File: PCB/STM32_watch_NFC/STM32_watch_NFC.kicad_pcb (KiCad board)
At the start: 2 copper layers, 40 x 40 mm, 68 parts, among them J1 Conn_01x06_Socket, J2 USB_C_Receptacle_PowerOnly_6P, Q1 2N7000, SW1 SW_DPST_x2, SW2 SW_DPST_x2, SW3 SW_DPST_x2, U1 STM32L031G6Ux, U2 MIC5365-3.3YC5, U3 ST25R3916-AQWT, U4 MT3608

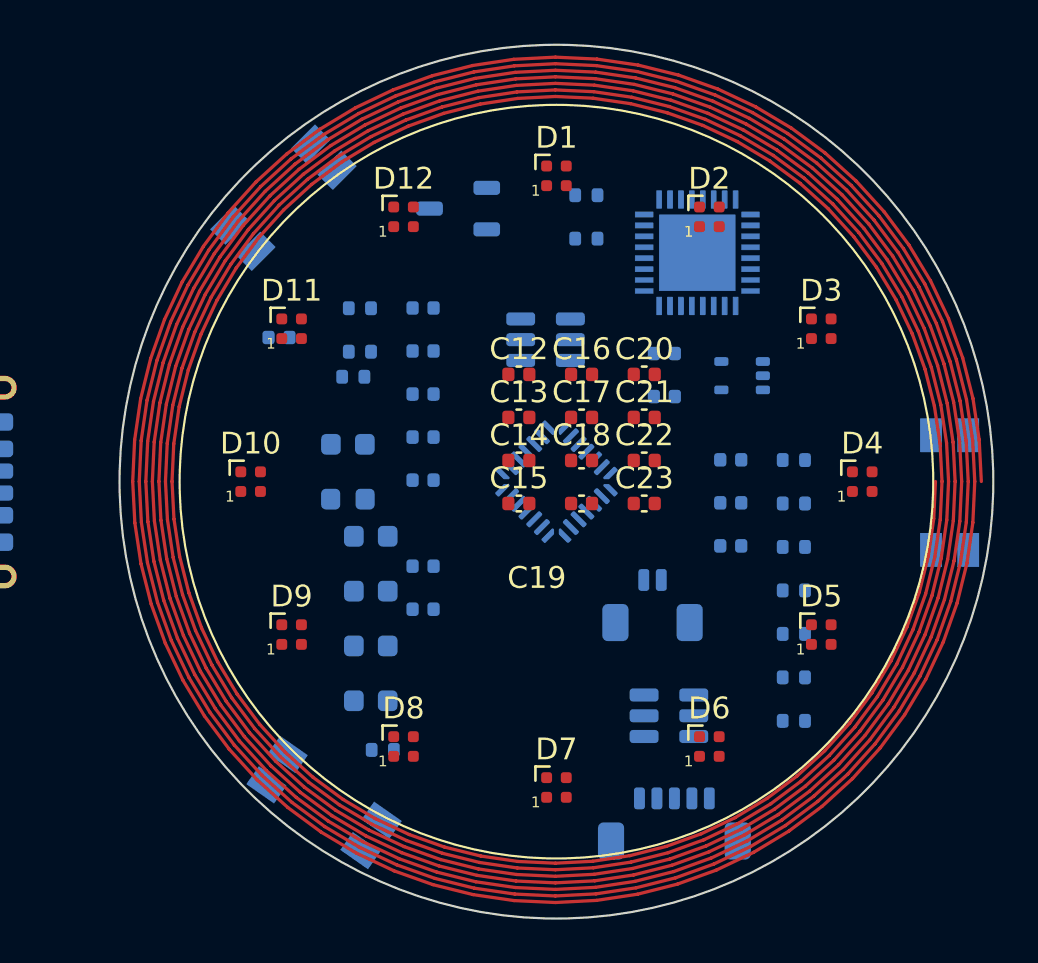
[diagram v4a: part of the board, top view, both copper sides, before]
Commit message: NFC antenna - Kicad
I hope that antenna will work - I used TI coil designer, st25r - antenna tunning program and lots of datasheets/aplication notes
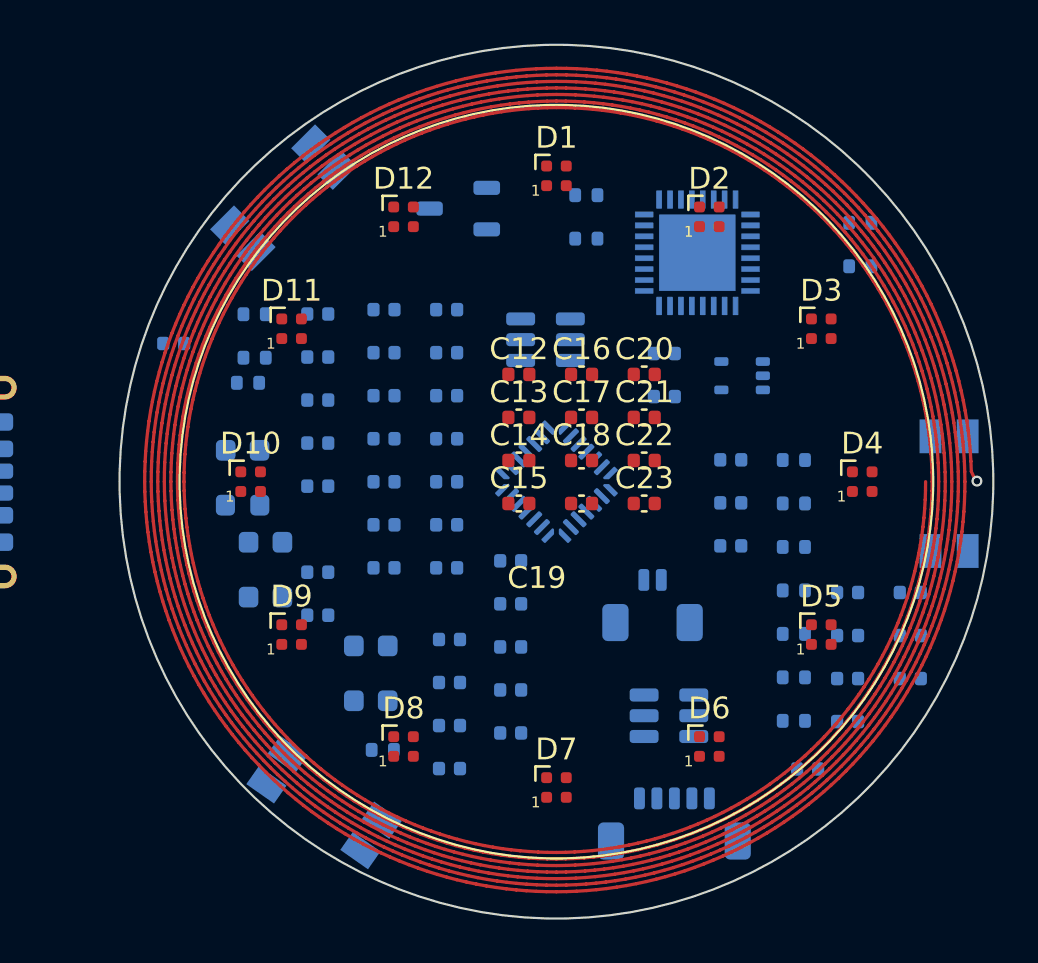
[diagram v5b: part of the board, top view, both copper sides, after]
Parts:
- added C31: 100n, Capacitor_SMD:C_0402_1005Metric, B.Cu at (143.5, 97.1)
- added C32: 22n, Capacitor_SMD:C_0402_1005Metric, B.Cu at (143.5, 99.1)
- added C33: 2.2uF, Capacitor_SMD:C_0402_1005Metric, B.Cu at (143.5, 101.1)
- added C34: 22n, Capacitor_SMD:C_0402_1005Metric, B.Cu at (143.5, 103.0)
- added C35: 2.2uF, Capacitor_SMD:C_0402_1005Metric, B.Cu at (143.5, 105.0)
- added C36: 22n, Capacitor_SMD:C_0402_1005Metric, B.Cu at (143.5, 107.0)
- added C37: 2.2uF, Capacitor_SMD:C_0402_1005Metric, B.Cu at (143.5, 108.9)
- added C38: 22n, Capacitor_SMD:C_0402_1005Metric, B.Cu at (140.6, 97.1)
- added C39: 2.2uF, Capacitor_SMD:C_0402_1005Metric, B.Cu at (140.6, 99.1)
- added C40: 22n, Capacitor_SMD:C_0402_1005Metric, B.Cu at (140.6, 101.1)
- added C41: 2.2uF, Capacitor_SMD:C_0402_1005Metric, B.Cu at (140.6, 103.0)
- added C42: 22n, Capacitor_SMD:C_0402_1005Metric, B.Cu at (140.6, 105.0)
- added C43: 2.2uF, Capacitor_SMD:C_0402_1005Metric, B.Cu at (140.6, 107.0)
- added C44: 22n, Capacitor_SMD:C_0402_1005Metric, B.Cu at (140.6, 108.9)
- added C45: 2.2uF, Capacitor_SMD:C_0402_1005Metric, B.Cu at (146.4, 108.6)
- added C46: 1u, Capacitor_SMD:C_0402_1005Metric, B.Cu at (146.4, 110.6)
- added C47: 22n, Capacitor_SMD:C_0402_1005Metric, B.Cu at (146.4, 112.6)
- added C48: 15pF, Capacitor_SMD:C_0402_1005Metric, B.Cu at (146.4, 114.5)
- added C49: 15pF, Capacitor_SMD:C_0402_1005Metric, B.Cu at (146.4, 116.5)
- added C50: 15pF, Capacitor_SMD:C_0402_1005Metric, B.Cu at (143.6, 112.2)
- added C51: 15pF, Capacitor_SMD:C_0402_1005Metric, B.Cu at (143.6, 114.2)
- added C52: 220pF, Capacitor_SMD:C_0402_1005Metric, B.Cu at (143.6, 116.2)
- added C53: 220pF, Capacitor_SMD:C_0402_1005Metric, B.Cu at (143.6, 118.1)
- added C54: 220pF, Capacitor_SMD:C_0402_1005Metric, B.Cu at (164.7, 110.1)
- added C55: 220pF, Capacitor_SMD:C_0402_1005Metric, B.Cu at (164.7, 112.0)
- added C56: 10pF, Capacitor_SMD:C_0402_1005Metric, B.Cu at (164.7, 114.0)
- added C57: 220pF, Capacitor_SMD:C_0402_1005Metric, B.Cu at (160.0, 118.2)
- added C58: 15pF, Capacitor_SMD:C_0402_1005Metric, B.Cu at (161.8, 110.1)
- added C59: 15pF, Capacitor_SMD:C_0402_1005Metric, B.Cu at (161.8, 112.0)
- added C60: 10pF, Capacitor_SMD:C_0402_1005Metric, B.Cu at (161.8, 114.0)
- added C61: 220pF, Capacitor_SMD:C_0402_1005Metric, B.Cu at (161.8, 116.0)
- added R16: 10K, Resistor_SMD:R_0402_1005Metric, B.Cu at (162.4, 93.2)
- added R17: 10K, Resistor_SMD:R_0402_1005Metric, B.Cu at (162.4, 95.1)
- moved C7 4.83 mm to (131.0, 98.7)
- moved C1 4.83 mm to (137.6, 97.3)
- moved C2 4.83 mm to (137.6, 99.3)
- moved C24 4.83 mm to (135.2, 107.8)
- moved C25 4.83 mm to (135.2, 110.3)
- moved C3 4.83 mm to (137.6, 101.3)
- moved C4 4.83 mm to (134.1, 103.6)
- moved C5 4.83 mm to (137.6, 103.2)
- moved C6 4.83 mm to (137.6, 105.2)
- moved C8 4.83 mm to (137.6, 109.1)
- moved C9 4.83 mm to (137.6, 111.1)
- moved FB1 4.83 mm to (134.1, 106.1)
- moved R1 4.83 mm to (134.7, 97.3)
- moved R2 4.83 mm to (134.7, 99.3)
- moved R3 4.83 mm to (134.4, 100.5)
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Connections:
- U1 pad 10: unconnected-(U1-PA4-Pad10) -> SPI_CS_STM
- U1 pad 11: unconnected-(U1-PA5-Pad11) -> SPI_SCL_STM
- U1 pad 12: unconnected-(U1-PA6-Pad12) -> SPI_MISO_STM
- U1 pad 13: unconnected-(U1-PA7-Pad13) -> SPI_MOSI_STM
- U1 pad 9: unconnected-(U1-PA3-Pad9) -> SPI_IRQ_STM
- U3 pad 1: unconnected-(U3-VDD_IO-Pad1) -> +3.3V
- U3 pad 10: unconnected-(U3-VDD_TX-Pad10) -> +5V
- U3 pad 11: unconnected-(U3-VDD_AM-Pad11) -> Net-(U3-VDD_AM)
- U3 pad 12: Net-(U3-GND_DR-Pad12) -> GND
- U3 pad 13: unconnected-(U3-RFO1-Pad13) -> Net-(U3-RFO1)
- U3 pad 14: unconnected-(U3-VDD_DR-Pad14) -> Net-(U3-VDD_DR)
- U3 pad 15: unconnected-(U3-RFO2-Pad15) -> Net-(U3-RFO2)
- U3 pad 16: Net-(U3-GND_DR-Pad12) -> GND
- U3 pad 20: unconnected-(U3-I2C_EN-Pad20) -> GND
- U3 pad 21: unconnected-(U3-VSS-Pad21) -> GND
- U3 pad 22: unconnected-(U3-RFI1-Pad22) -> Net-(U3-RFI1)
- U3 pad 23: unconnected-(U3-RFI2-Pad23) -> Net-(U3-RFI2)
- U3 pad 24: unconnected-(U3-AGDC-Pad24) -> Net-(U3-AGDC)
- U3 pad 26: unconnected-(U3-GND_A-Pad26) -> GND
- U3 pad 27: unconnected-(U3-IRQ-Pad27) -> SPI_IRQ_STM
- U3 pad 29: unconnected-(U3-~{BSS}-Pad29) -> SPI_CS_STM
- U3 pad 3: unconnected-(U3-VDD_D-Pad3) -> Net-(U3-VDD_D)
- U3 pad 30: unconnected-(U3-SCLK/SCL-Pad30) -> SPI_SCL_STM
- U3 pad 31: unconnected-(U3-MOSI-Pad31) -> SPI_MOSI_STM
- U3 pad 32: unconnected-(U3-MISO/SDA-Pad32) -> SPI_MISO_STM
- U3 pad 33: unconnected-(U3-EXP-Pad33) -> GND
- U3 pad 4: unconnected-(U3-XTO-Pad4) -> Net-(U3-XTO)
- U3 pad 5: unconnected-(U3-XTI-Pad5) -> Net-(U3-XTI)
- U3 pad 6: unconnected-(U3-GND_D-Pad6) -> GND
- U3 pad 7: unconnected-(U3-VDD_A-Pad7) -> Net-(U3-VDD_A)
- U3 pad 8: unconnected-(U3-VDD-Pad8) -> +5V
- U3 pad 9: unconnected-(U3-VDD_RF-Pad9) -> Net-(U3-VDD_DR)
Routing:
- net unconnected-(U4-NC-Pad6): track 811.2 -> 789.5 mm
- net /NFC_RFID/A1: vias 0 -> 1

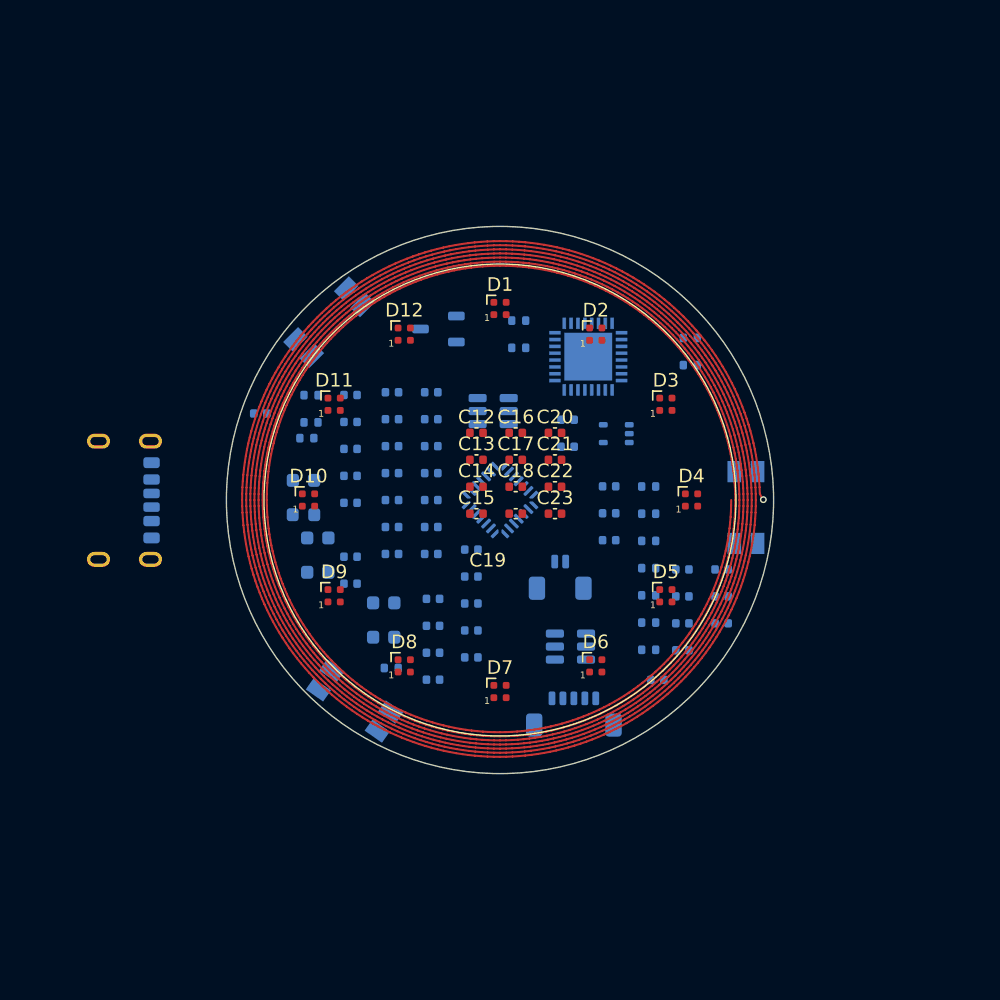
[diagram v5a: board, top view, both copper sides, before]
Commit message: Kicad - LCSC, footprints
I managed to add all (I hope so :) ) LCSC values - which component will be used. With that I could determine all footprints
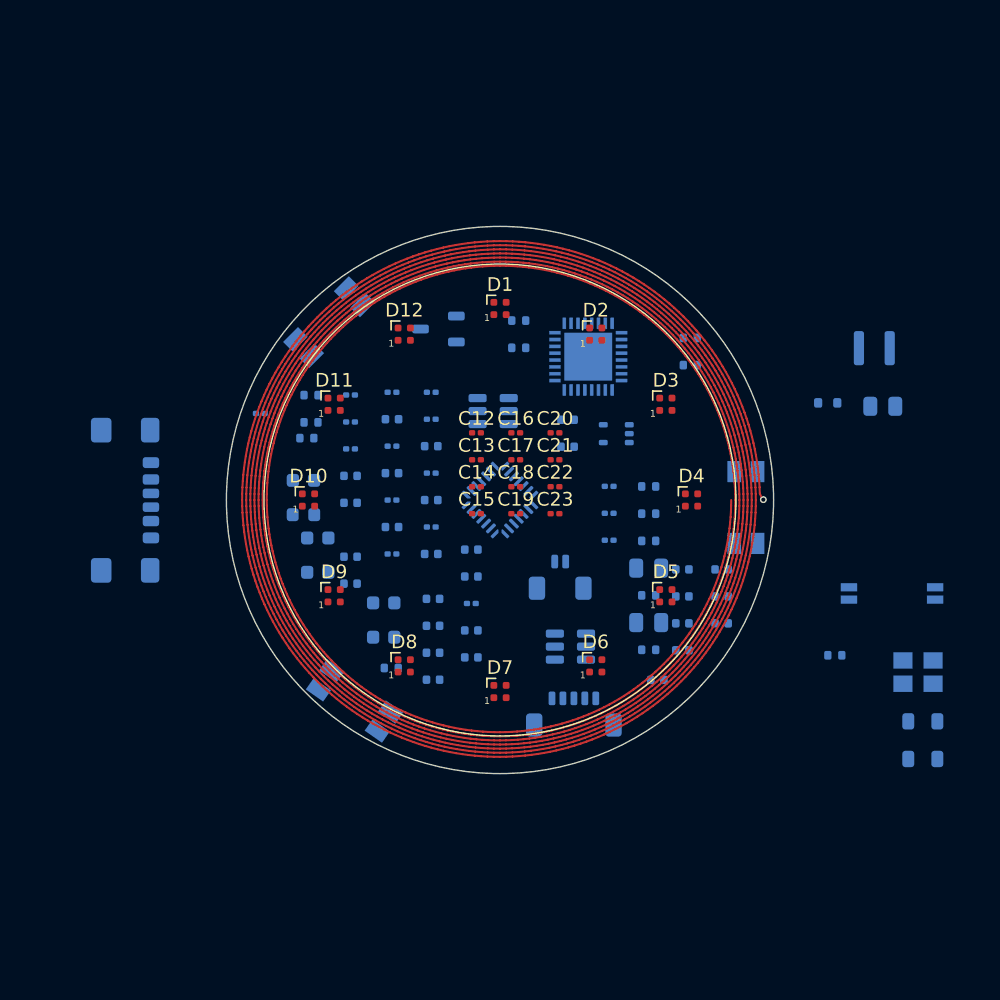
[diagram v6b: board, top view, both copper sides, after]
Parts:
- added D13: D_Schottky, Diode_SMD:D_SOD-523, B.Cu at (172.5, 97.9)
- added L1: 22uH, Components:SLW3015, B.Cu at (175.9, 93.9)
- added L2: 270nH 500mOhm, Inductor_SMD:L_0805_2012Metric, B.Cu at (179.4, 121.2)
- added L3: 270nH 500mOhm, Inductor_SMD:L_0805_2012Metric, B.Cu at (179.4, 123.9)
- added R8: 16.5K, Resistor_SMD:R_0805_2012Metric, B.Cu at (176.5, 98.2)
- added R9: 2.2K, Resistor_SMD:R_0402_1005Metric, B.Cu at (173.0, 116.3)
- added Y1: 27.12Mhz, Crystal:Crystal_SMD_3225-4Pin_3.2x2.5mm, B.Cu at (179.1, 117.6)
- added Y2: 32.768kHz, Crystal:Crystal_SMD_SeikoEpson_MC146-4Pin_6.7x1.5mm, B.Cu at (177.2, 111.8)
- C1, C12, C13, C14, C15, C16, C17, C18, C19, C2, C20, C21, C22, C23, C28, C29, C3, C30, C31, C32, C34, C36, C38, C40, C42, C44, C47, C7: footprint Capacitor_SMD:C_0402_1005Metric -> Capacitor_SMD:C_0201_0603Metric
- C26, C27: value 22u -> 10u
- J2: footprint Connector_USB:USB_C_Receptacle_GCT_USB4125-xx-x-0190_6P_TopMnt_Horizontal -> Connector_USB:USB_C_Receptacle_GCT_USB4135-GF-A_6P_TopMnt_Horizontal
- R11, R15, R6: value 500 -> 510
- R12, R14: footprint Resistor_SMD:R_0402_1005Metric -> Resistor_SMD:R_0805_2012Metric

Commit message: Kicad - layout
I placed all components in logical way. It is NOT routed.
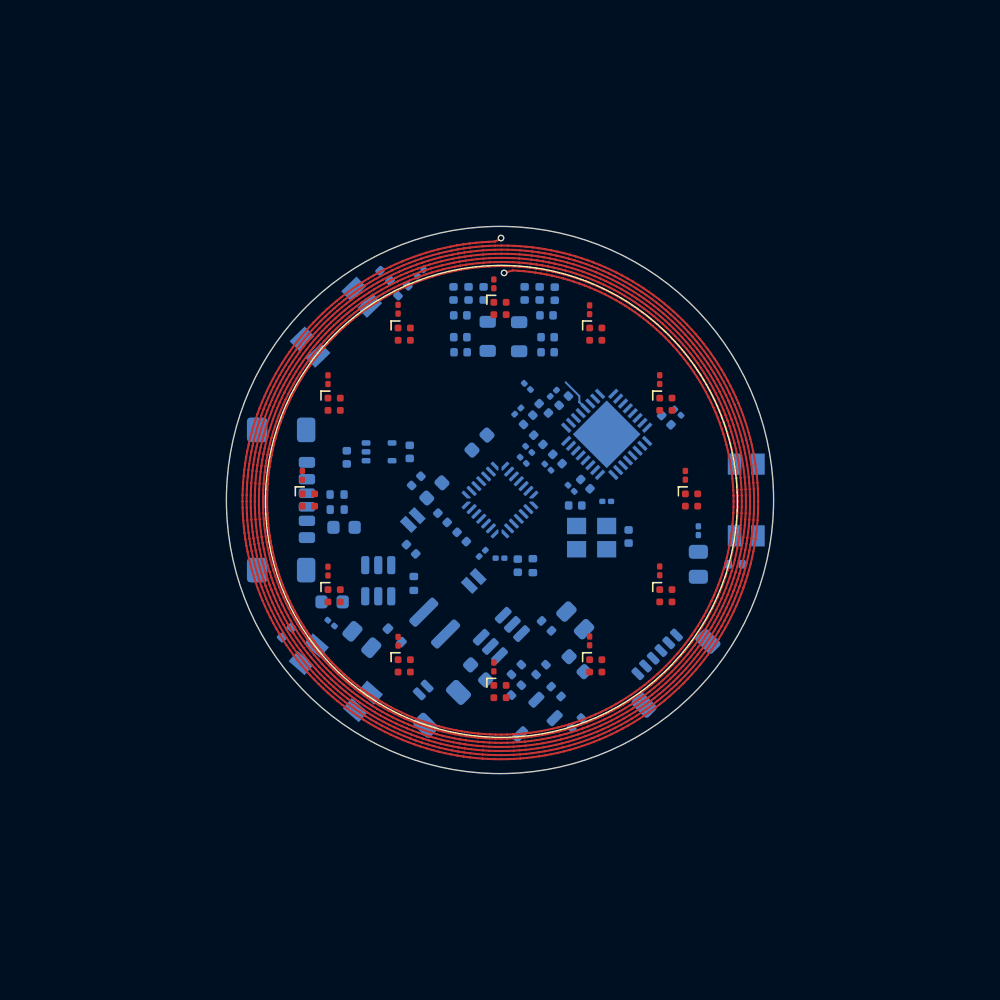
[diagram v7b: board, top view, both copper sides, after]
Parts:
- removed C32: 22n, Capacitor_SMD:C_0201_0603Metric
- removed C33: 2.2uF, Capacitor_SMD:C_0402_1005Metric
- C3: footprint Capacitor_SMD:C_0201_0603Metric -> Capacitor_SMD:C_0402_1005Metric
- J1: footprint Connector_JST:JST_SUR_SM05B-SURS-TF_1x05-1MP_P0.80mm_Horizontal -> Connector_JST:JST_SUR_SM06B-SURS-TF_1x06-1MP_P0.80mm_Horizontal
- moved L3 44.3 mm to (147.6, 93.0), turned to -90 degrees
- moved L2 40.8 mm to (149.9, 93.1), turned to 90 degrees
- moved L1 37.9 mm to (143.7, 114.0), turned to -45 degrees
- moved D13 35.9 mm to (140.8, 114.9), turned to -45 degrees
- moved SW2 33.2 mm to (166.5, 105.0), turned to 90 degrees
- moved Y2 33.0 mm to (144.4, 108.7), turned to 135 degrees
- moved SW1 32.5 mm to (136.5, 118.0), turned to -41 degrees
- moved C56 30.4 mm to (146.2, 89.9), turned to 90 degrees
- moved C57 30.3 mm to (145.6, 91.5), turned to 0 degrees
- moved Q1 29.5 mm to (150.9, 121.2), turned to -135 degrees
- moved R2 29.3 mm to (154.1, 121.3), turned to -135 degrees
- moved R1 28.1 mm to (152.6, 119.0), turned to 135 degrees
- moved SW3 27.7 mm to (136.5, 92.0), turned to -136 degrees
- moved R8 27.4 mm to (154.0, 113.8), turned to 135 degrees
- moved R16 27.4 mm to (149.7, 117.4), turned to 45 degrees
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- renumbered C17 to C12, C20 to C13, C21 to C14, C13 to C15, C14 to C16, C23 to C17, C22 to C18, C18 to C19, C15 to C20, C19 to C21, C12 to C22, C16 to C23
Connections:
- D12 pad 1: unconnected-(D12-DOUT-Pad1) -> Net-(D1-DIN)
- D6 pad 1: Net-(D6-DOUT) -> unconnected-(D6-DOUT-Pad1)
- D7 pad 3: Net-(D6-DOUT) -> Net-(D7-DIN)
- R6 pad 2: Net-(D1-DIN) -> Net-(D7-DIN)
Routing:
- net Net-(U3-RFO1): track 0.00 -> 2.50 mm
- net /NFC_RFID/A2: vias 0 -> 1
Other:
- copper layers 2 -> 4
